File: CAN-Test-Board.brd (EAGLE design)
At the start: 52.3 x 59.4 mm, 52 parts, among them Y1 ECS-80-S-4X, Y2 ECS-80-S-4X

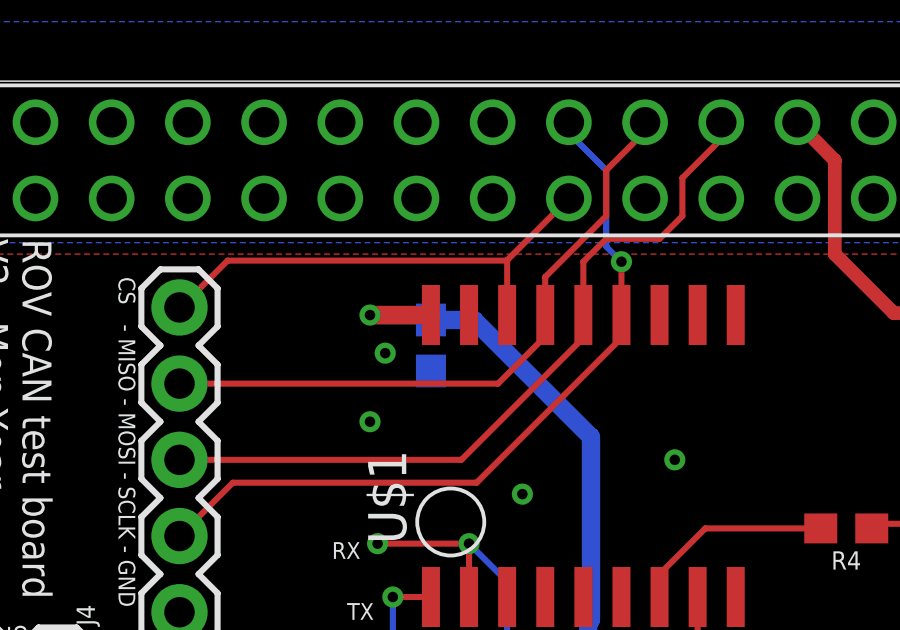
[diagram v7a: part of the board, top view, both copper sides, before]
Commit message: Shorted Reset to 3V3 instead of leaving it floating
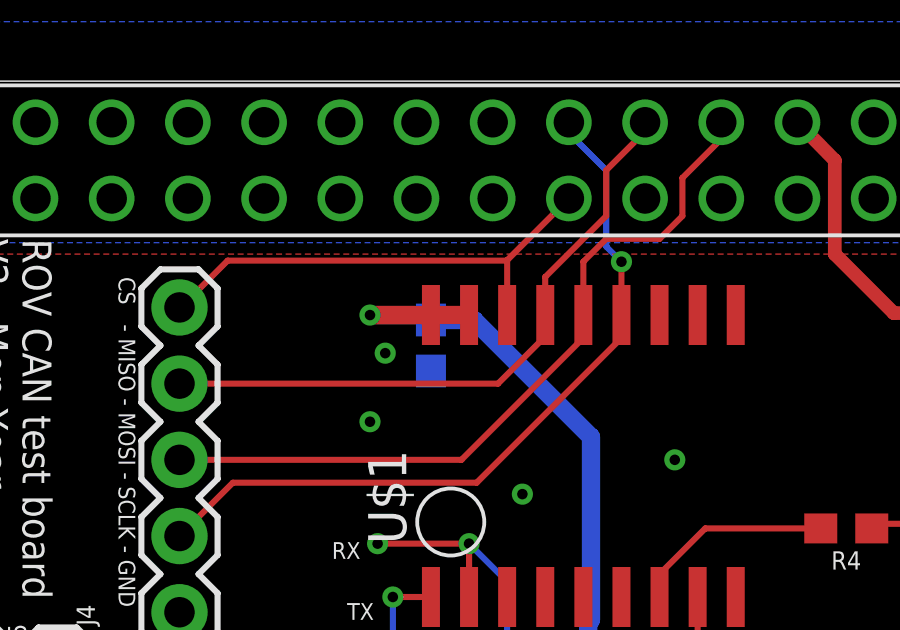
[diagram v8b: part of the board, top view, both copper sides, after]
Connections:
- removed net RESET: U$1.RESET
- net 3V3: now also U$1.RESET
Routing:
- net 3V3: track 170.0 -> 171.3 mm
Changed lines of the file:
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@@
 <via x="37.338" y="53.086" extent="1-16" drill="0.35"/>
 <contactref element="RESET" pad="1"/>
-<wire x1="40.1574" y1="57.9882" x2="45.2374" y2="55.4482" width="0" layer="19" extent="1-1"/>
-<wire x1="37.338" y1="53.086" x2="40.1574" y2="57.9882" width="0" layer="19" extent="1-1"/>
-<wire x1="36.068" y1="50.546" x2="37.338" y2="53.086" width="0" layer="19" extent="1-1"/>
-<wire x1="34.29" y1="48.475" x2="36.068" y2="50.546" width="0" layer="19" extent="1-1"/>
-<wire x1="35.0774" y1="55.4482" x2="37.338" y2="53.086" width="0" layer="19" extent="1-1"/>
-<wire x1="27.4574" y1="55.4482" x2="35.0774" y2="55.4482" width="0" layer="19" extent="1-1"/>
-<wire x1="19.8374" y1="57.9882" x2="27.4574" y2="55.4482" width="0" layer="19" extent="1-1"/>
-<wire x1="14.7574" y1="55.4482" x2="19.8374" y2="57.9882" width="0" layer="19" extent="1-1"/>
-<wire x1="9.6774" y1="55.4482" x2="14.7574" y2="55.4482" width="0" layer="19" extent="1-1"/>
-<wire x1="16.256" y1="50.292" x2="14.7574" y2="55.4482" width="0" layer="19" extent="1-1"/>
-<wire x1="17.78" y1="49.696" x2="16.256" y2="50.292" width="0" layer="19" extent="16-16"/>
-<wire x1="15.748" y1="48.006" x2="16.256" y2="50.292" width="0" layer="19" extent="1-1"/>
-<wire x1="20.828" y1="45.593" x2="17.78" y2="49.696" width="0" layer="19" extent="16-16"/>
-<wire x1="25.908" y1="46.736" x2="20.828" y2="45.593" width="0" layer="19" extent="1-1"/>
-<wire x1="27.94" y1="42.164" x2="25.908" y2="46.736" width="0" layer="19" extent="1-1"/>
-<wire x1="3.302" y1="54.991" x2="9.6774" y2="55.4482" width="0" layer="19" extent="1-1"/>
-<wire x1="3.302" y1="56.7436" x2="3.302" y2="56.7436" width="0" layer="19" extent="1-16"/>
-<wire x1="2.0574" y1="57.9882" x2="3.302" y2="56.7436" width="0" layer="19" extent="1-1"/>
-<wire x1="17.78" y1="39.624" x2="20.828" y2="45.593" width="0" layer="19" extent="16-16"/>
-<wire x1="18.796" y1="37.084" x2="17.78" y2="39.624" width="0" layer="19" extent="16-16"/>
-<wire x1="14.732" y1="37.338" x2="17.78" y2="39.624" width="0" layer="19" extent="16-16"/>
-<wire x1="22.606" y1="36.742" x2="18.796" y2="37.084" width="0" layer="19" extent="16-16"/>
-<wire x1="13.208" y1="32.004" x2="14.732" y2="37.338" width="0" layer="19" extent="1-1"/>
-<wire x1="13.12" y1="29.464" x2="13.208" y2="32.004" width="0" layer="19" extent="1-1"/>
-<wire x1="11.43" y1="26.416" x2="13.12" y2="29.464" width="0" layer="19" extent="1-1"/>
-<wire x1="12.7" y1="23.622" x2="11.43" y2="26.416" width="0" layer="19" extent="1-1"/>
-<wire x1="14.986" y1="20.994" x2="12.7" y2="23.622" width="0" layer="19" extent="16-16"/>
-<wire x1="16.764" y1="20.994" x2="14.986" y2="20.994" width="0" layer="19" extent="16-16"/>
-<wire x1="18.796" y1="20.994" x2="16.764" y2="20.994" width="0" layer="19" extent="16-16"/>
-<wire x1="21.082" y1="22.352" x2="20.574" y2="20.994" width="0" layer="19" extent="1-16"/>
-<wire x1="22.036" y1="21.626" x2="22.036" y2="22.426" width="0" layer="19" extent="1-1"/>
-<wire x1="14.986" y1="18.376" x2="14.986" y2="20.994" width="0" layer="19" extent="16-16"/>
-<wire x1="13.536" y1="16.826" x2="14.986" y2="18.376" width="0" layer="19" extent="1-16"/>
-<wire x1="13.208" y1="14.986" x2="13.536" y2="16.826" width="0" layer="19" extent="1-1"/>
-<wire x1="8.636" y1="23.368" x2="12.7" y2="23.622" width="0" layer="19" extent="1-1"/>
-<wire x1="6.35" y1="20.574" x2="8.636" y2="23.368" width="0" layer="19" extent="1-1"/>
-<wire x1="4.318" y1="21.082" x2="6.35" y2="20.574" width="0" layer="19" extent="1-1"/>
-<wire x1="9.652" y1="18.796" x2="6.35" y2="20.574" width="0" layer="19" extent="1-1"/>
-<wire x1="4.826" y1="16.51" x2="6.35" y2="20.574" width="0" layer="19" extent="1-1"/>
-<wire x1="8.89" y1="32.893" x2="13.208" y2="32.004" width="0" layer="19" extent="1-1"/>
-<wire x1="5.08" y1="26.416" x2="8.636" y2="23.368" width="0" layer="19" extent="1-1"/>
-<wire x1="3.937" y1="32.512" x2="8.89" y2="32.893" width="0" layer="19" extent="1-1"/>
-<wire x1="29.464" y1="24.892" x2="24.13" y2="21.844" width="0" layer="19" extent="1-1"/>
-<wire x1="29.464" y1="26.582" x2="29.464" y2="24.892" width="0" layer="19" extent="16-16"/>
-<wire x1="32.258" y1="26.924" x2="29.464" y2="26.582" width="0" layer="19" extent="16-16"/>
-<wire x1="34.798" y1="27.686" x2="32.258" y2="26.924" width="0" layer="19" extent="16-16"/>
-<wire x1="35.56" y1="30.988" x2="34.798" y2="27.686" width="0" layer="19" extent="1-1"/>
-<wire x1="30.734" y1="30.988" x2="32.258" y2="26.924" width="0" layer="19" extent="16-16"/>
-<wire x1="30.607" y1="33.909" x2="30.734" y2="30.988" width="0" layer="19" extent="1-1"/>
-<wire x1="34.29" y1="35.726" x2="30.607" y2="33.909" width="0" layer="19" extent="1-1"/>
-<wire x1="25.996" y1="29.464" x2="29.464" y2="26.582" width="0" layer="19" extent="1-16"/>
-<wire x1="35.814" y1="22.098" x2="34.798" y2="27.686" width="0" layer="19" extent="1-1"/>
-<wire x1="36.068" y1="18.796" x2="35.814" y2="22.098" width="0" layer="19" extent="1-1"/>
-<wire x1="36.068" y1="16.256" x2="36.068" y2="18.796" width="0" layer="19" extent="1-1"/>
-<wire x1="36.068" y1="13.716" x2="36.068" y2="16.256" width="0" layer="19" extent="1-1"/>
-<wire x1="36.068" y1="11.176" x2="36.068" y2="13.716" width="0" layer="19" extent="1-1"/>
-<wire x1="33.02" y1="7.366" x2="36.068" y2="11.176" width="0" layer="19" extent="1-1"/>
-<wire x1="33.652" y1="3.296" x2="33.02" y2="7.366" width="0" layer="19" extent="1-1"/>
-<wire x1="27.94" y1="3.268" x2="33.652" y2="3.296" width="0" layer="19" extent="1-1"/>
-<wire x1="24.892" y1="3.268" x2="27.94" y2="3.268" width="0" layer="19" extent="1-1"/>
-<wire x1="22.987" y1="6.223" x2="24.892" y2="3.268" width="0" layer="19" extent="1-1"/>
-<wire x1="22.186" y1="8.636" x2="22.987" y2="6.223" width="0" layer="19" extent="16-16"/>
-<wire x1="41.402" y1="8.636" x2="36.068" y2="11.176" width="0" layer="19" extent="1-1"/>
-<wire x1="39.652" y1="3.296" x2="41.402" y2="8.636" width="0" layer="19" extent="1-1"/>
-<wire x1="7.786" y1="38.989" x2="8.89" y2="32.893" width="0" layer="19" extent="1-1"/>
-<wire x1="5.334" y1="39.878" x2="7.786" y2="38.989" width="0" layer="19" extent="1-1"/>
-<wire x1="2.667" y1="39.878" x2="5.334" y2="39.878" width="0" layer="19" extent="1-1"/>
-<wire x1="9.398" y1="41.656" x2="7.786" y2="38.989" width="0" layer="19" extent="1-1"/>
-<wire x1="41.998" y1="31.115" x2="35.56" y2="30.988" width="0" layer="19" extent="1-1"/>
-<wire x1="42.672" y1="34.102" x2="41.998" y2="31.115" width="0" layer="19" extent="1-1"/>
-<wire x1="44.958" y1="34.378" x2="42.672" y2="34.102" width="0" layer="19" extent="1-1"/>
-<wire x1="44.704" y1="28.448" x2="41.998" y2="31.115" width="0" layer="19" extent="1-1"/>
-<wire x1="44.45" y1="23.114" x2="44.704" y2="28.448" width="0" layer="19" extent="1-1"/>
-<wire x1="42.418" y1="22.264" x2="44.45" y2="23.114" width="0" layer="19" extent="16-16"/>
-<wire x1="9.398" y1="8.382" x2="13.208" y2="14.986" width="0" layer="19" extent="1-1"/>
-<wire x1="6.096" y1="6.858" x2="9.398" y2="8.382" width="0" layer="19" extent="1-1"/>
-<wire x1="5.08" y1="8.89" x2="6.096" y2="6.858" width="0" layer="19" extent="1-1"/>
-<wire x1="2.286" y1="2.54" x2="6.096" y2="6.858" width="0" layer="19" extent="1-1"/>
-<wire x1="12.954" y1="3.048" x2="9.398" y2="8.382" width="0" layer="19" extent="1-1"/>
-<wire x1="49.784" y1="2.286" x2="39.652" y2="3.296" width="0" layer="19" extent="1-1"/>
-<wire x1="12.494" y1="8.001" x2="2.286" y2="2.54" width="0" layer="19" extent="1-1"/>
 </signal>
 <signal name="CAN_H" class="1">
@@
 <contactref element="D1" pad="A"/>
 <wire x1="27.94" y1="8.04" x2="27.94" y2="5.418" width="0.3048" layer="1"/>
-</signal>
-<signal name="RESET">
-<contactref element="U$1" pad="RESET"/>
 </signal>
 <signal name="OSC1" class="1">
@@
 <wire x1="14.478" y1="39.624" x2="12.065" y2="37.211" width="0.6096" layer="1"/>
 <wire x1="9.652" y1="30.48" x2="2.286" y2="30.48" width="0.6096" layer="1"/>
+<contactref element="U$1" pad="RESET"/>
+<wire x1="17.78" y1="51.564" x2="19.05" y2="51.564" width="0.6096" layer="1"/>
 </signal>
 <signal name="N$3">
